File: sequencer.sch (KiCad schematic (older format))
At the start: 0 parts

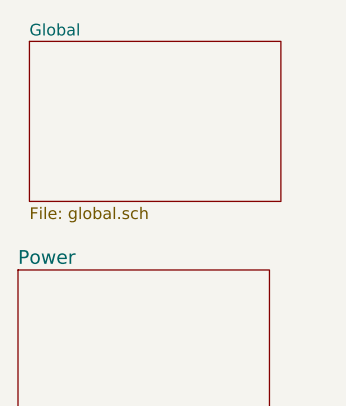
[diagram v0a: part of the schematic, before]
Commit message: updated component values and revision
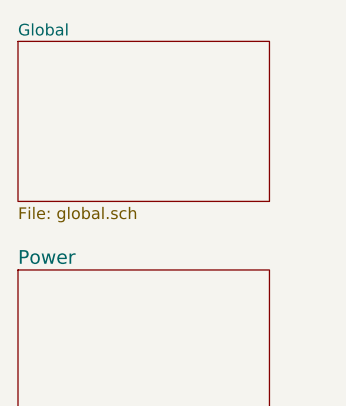
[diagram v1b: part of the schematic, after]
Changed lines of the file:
@@
 Sheet 1 8
 Title "PER|FORMER eurorack sequencer"
-Date "2018-10-09"
-Rev "1.0"
+Date "2019-04-10"
+Rev "1.1"
 Comp "westlicht"
 Comment1 "cc-by-nc-sa"
@@
 $EndDescr
 $Sheet
-S 750  700  1100 700
+S 700  700  1100 700
 U 5AF89FF5
 F0 "Global" 51
